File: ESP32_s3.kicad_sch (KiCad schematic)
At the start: 77 parts, among them J1 Conn_01x02_Pin, J10 TXRX2, J11 backup, J12 Conn_01x02_Pin, J13 jetsonnano, J14 Conn_01x03_Pin, J15 Conn_01x03_Pin, J2 programming header usb, J3 Conn_01x02, J4 Servo motor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

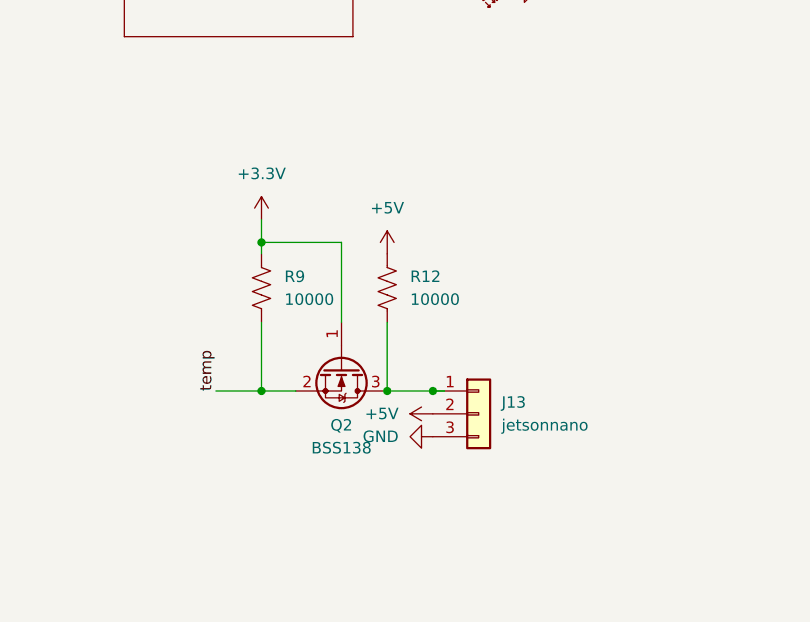
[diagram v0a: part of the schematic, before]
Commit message: Finished PCB Boost Layout
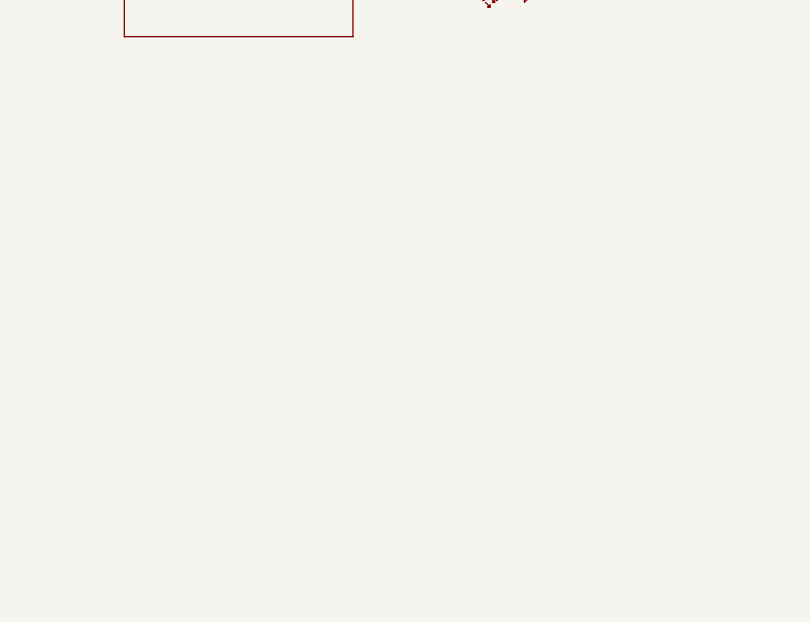
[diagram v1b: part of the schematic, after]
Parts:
- removed J13: jetsonnano, 61300311121:61300311121, symbol Connector_Generic:Conn_01x03
- removed Q2: BSS138, Package_TO_SOT_SMD:SOT-23, symbol Transistor_FET:BSS138
- removed R12, R9: 10000, RR1220P-1030-D:RESC2012X50N, symbol Device:R_US

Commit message: PCB update
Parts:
- added J13: Jetson Power Supply, 01x02connector:CONN_61300211121_WRE, symbol Connector:Conn_01x02_Pin
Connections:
- net +5V: no longer D10.1 (K), R11.1
- new net 5V: D10.1 (K), J13.1 (Pin_1), J13.2 (Pin_2), R11.1
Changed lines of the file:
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@@
 	)
 	(junction
+		(at 66.04 74.93)
+		(diameter 0)
+		(color 0 0 0 0)
+	)
+	(junction
 		(at 95.25 149.86)
 		(diameter 0)
@@
 	(wire
 		(pts
+			(xy 63.5 74.93) (xy 66.04 74.93)
+		)
+		(stroke
+			(width 0)
+			(type default)
+		)
+	)
+	(wire
+		(pts
 			(xy 254 215.9) (xy 248.92 215.9)
 		)
@@
 	(wire
 		(pts
+			(xy 66.04 76.2) (xy 66.04 74.93)
+		)
+		(stroke
+			(width 0)
+			(type default)
+		)
+	)
+	(wire
+		(pts
 			(xy 224.79 52.07) (xy 213.36 52.07)
 		)
@@
 	(wire
 		(pts
+			(xy 66.04 76.2) (xy 73.66 76.2)
+		)
+		(stroke
+			(width 0)
+			(type default)
+		)
+	)
+	(wire
+		(pts
 			(xy 182.88 152.4) (xy 180.34 152.4)
 		)
@@
 	(wire
 		(pts
+			(xy 66.04 74.93) (xy 66.04 73.66)
+		)
+		(stroke
+			(width 0)
+			(type default)
+		)
+	)
+	(wire
+		(pts
 			(xy 203.2 187.96) (xy 208.28 187.96)
 		)
@@
 	(wire
 		(pts
+			(xy 66.04 73.66) (xy 73.66 73.66)
+		)
+		(stroke
+			(width 0)
+			(type default)
+		)
+	)
+	(wire
+		(pts
 			(xy 133.35 36.83) (xy 146.05 36.83)
 		)
@@
 		)
 	)
+	(global_label "5V"
+		(shape input)
+		(at 63.5 74.93 180)
+		(fields_autoplaced yes)
+		(effects
+			(font
+				(size 1.27 1.27)
+			)
+			(justify right)
+		)
+		(property "Intersheetrefs" "${INTERSHEET_REFS}"
+			(at 58.2167 74.93 0)
+			(effects
+				(font
+					(size 1.27 1.27)
+				)
+				(justify right)
+				(hide yes)
+			)
+		)
+	)
 	(global_label "Vout"
 		(shape input)
@@
 		)
 	)
+	(global_label "5V"
+		(shape input)
+		(at 96.52 49.53 0)
+		(fields_autoplaced yes)
+		(effects
+			(font
+				(size 1.27 1.27)
+			)
+			(justify left)
+		)
+		(property "Intersheetrefs" "${INTERSHEET_REFS}"
+			(at 101.8033 49.53 0)
+			(effects
+				(font
+					(size 1.27 1.27)
+				)
+				(justify left)
+				(hide yes)
+			)
+		)
+	)
 	(global_label "Vin"
 		(shape input)
@@
 	)
 	(symbol
-		(lib_id "stm32f091-rescue:+5V-power")
-		(at 96.52 49.53 270)
-		(unit 1)
-		(exclude_from_sim no)
-		(in_bom yes)
-		(on_board yes)
-		(dnp no)
-		(property "Reference" "#PWR021"
-			(at 92.71 49.53 0)
-			(effects
-				(font
-					(size 1.27 1.27)
-				)
-				(hide yes)
-			)
-		)
-		(property "Value" "+5V"
-			(at 100.9142 49.911 0)
-			(effects
-				(font
-					(size 1.27 1.27)
-				)
-			)
-		)
-		(property "Footprint" ""
-			(at 96.52 49.53 0)
-			(effects
-				(font
-					(size 1.27 1.27)
-				)
-				(hide yes)
-			)
-		)
-		(property "Datasheet" ""
-			(at 96.52 49.53 0)
-			(effects
-				(font
-					(size 1.27 1.27)
-				)
-				(hide yes)
-			)
-		)
-		(property "Description" ""
-			(at 96.52 49.53 0)
-			(effects
-				(font
-					(size 1.27 1.27)
-				)
-				(hide yes)
-			)
-		)
-		(pin "1"
-		)
-		(instances
-			(project "ESP32_s3"
-				(path "/17b1a26b-4dd3-45da-ac9f-9f7d4372170f"
-					(reference "#PWR021")
-					(unit 1)
-				)
-			)
-		)
-	)
-	(symbol
 		(lib_id "Device:C")
 		(at 270.51 44.45 0)
@@
 					(unit 1)
 				)
+			)
+		)
+	)
+	(symbol
+		(lib_id "Connector:Conn_01x02_Pin")
+		(at 78.74 76.2 180)
+		(unit 1)
+		(exclude_from_sim no)
+		(in_bom yes)
+		(on_board yes)
+		(dnp no)
+		(property "Reference" "J13"
+			(at 80.01 73.6599 0)
+			(effects
+				(font
+					(size 1.27 1.27)
+				)
+				(justify right)
+				(hide yes)
+			)
+		)
+		(property "Value" "Jetson Power Supply"
+			(at 80.264 74.93 0)
+			(effects
+				(font
+					(size 1.27 1.27)
+				)
+				(justify right)
+			)
+		)
+		(property "Footprint" "01x02connector:CONN_61300211121_WRE"
+			(at 78.74 76.2 0)
+			(effects
+				(font
+					(size 1.27 1.27)
+				)
+				(hide yes)
+			)
+		)
+		(property "Datasheet" "~"
+			(at 78.74 76.2 0)
+			(effects
+				(font
+					(size 1.27 1.27)
+				)
+				(hide yes)
+			)
+		)
+		(property "Description" "Generic connector, single row, 01x02, script generated"
+			(at 78.74 76.2 0)
+			(effects
+				(font
+					(size 1.27 1.27)
+				)
+				(hide yes)
+			)
+		)
+		(pin "1"
+		)
+		(pin "2"
+		)
+		(instances
+			(project "ESP32_s3"
+				(path "/17b1a26b-4dd3-45da-ac9f-9f7d4372170f"
+					(reference "J13")
+					(unit 1)
+				)

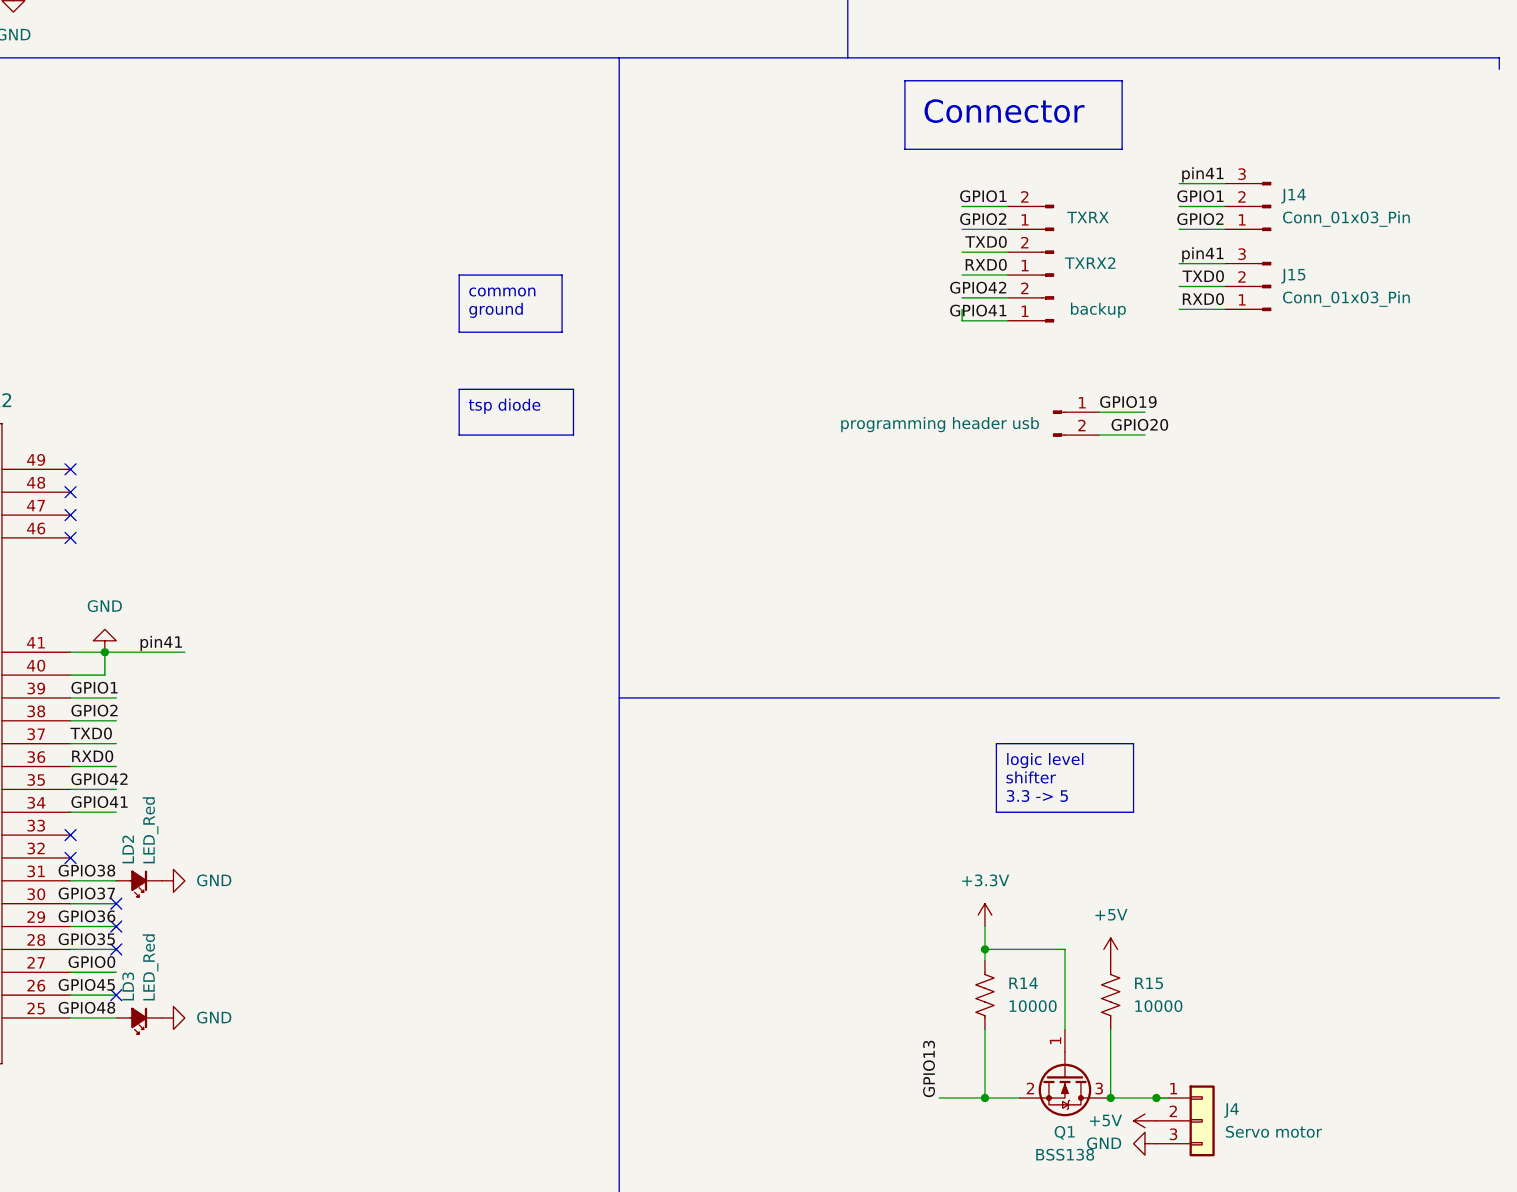
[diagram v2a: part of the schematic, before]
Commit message: add resistors to debugging led
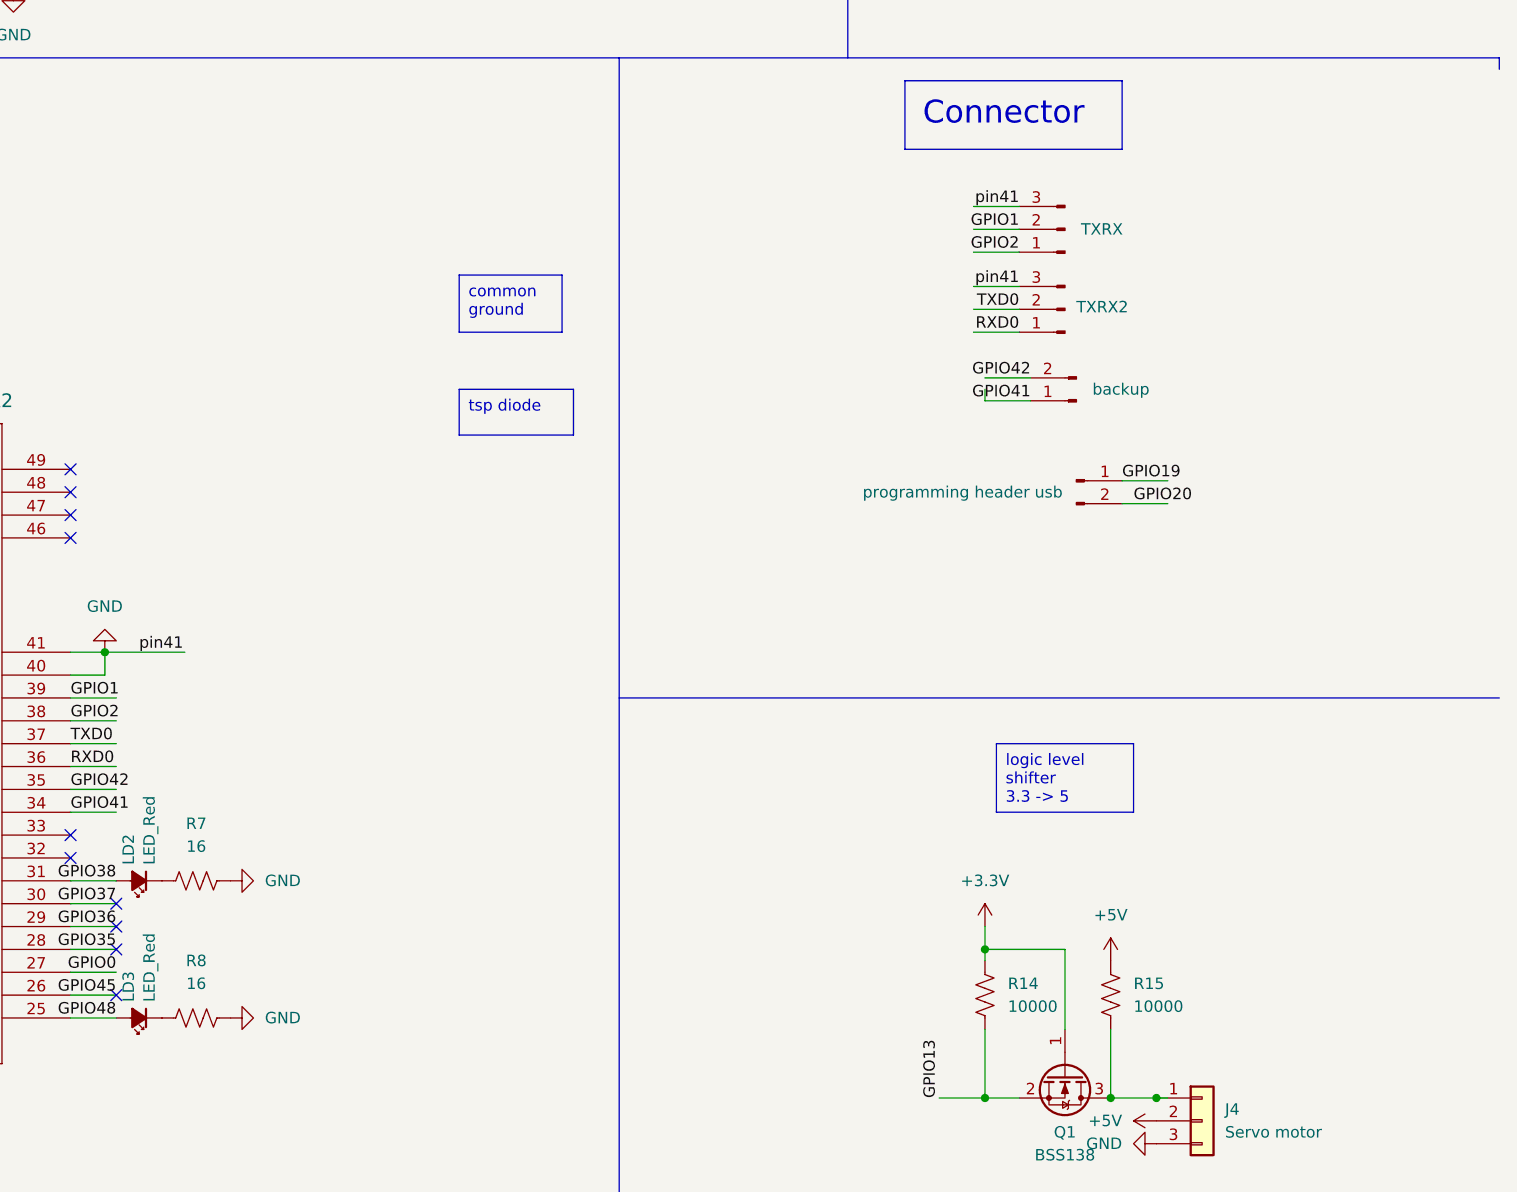
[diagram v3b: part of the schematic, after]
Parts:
- removed J10: TXRX2, 01x02connector:CONN_61300211121_WRE, symbol Connector:Conn_01x02_Pin
- removed J6: TXRX, 01x02connector:CONN_61300211121_WRE, symbol Connector:Conn_01x02_Pin
- added R7, R8: 16, CRGCQ0805F220R:RESC2012X65N, symbol Device:R_US
- J14: value Conn_01x03_Pin -> TXRX
- J15: value Conn_01x03_Pin -> TXRX2
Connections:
- net GND: now also R7.2, R8.2; no longer LD2.1 (K), LD3.1 (K)
- new net: LD2.1 (K), R7.1
- new net: LD3.1 (K), R8.1

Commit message: update PCB layout
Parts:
- R10, R4: value 0 -> 10k; footprint RMCF1206ZR0R00:RESC3216X70N -> CRCW080535K7FKEA:RESC2012X50N
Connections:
- net +3.3V: now also R10.2, R4.2; no longer C14.1, C2.1, R10.1, R4.1, SW1.2, SW2.2
- net EN: now also C14.1, R10.1, SW1.2; no longer R10.2
- net GPIO0: now also C2.1, R4.1, SW2.2; no longer R4.2
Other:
- moved on the sheet: R10, R4
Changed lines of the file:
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@@
 	)
 	(junction
+		(at 361.95 36.83)
+		(diameter 0)
+		(color 0 0 0 0)
+	)
+	(junction
 		(at 289.56 67.31)
 		(diameter 0)
@@
 	)
 	(junction
+		(at 361.95 60.96)
+		(diameter 0)
+		(color 0 0 0 0)
+	)
+	(junction
 		(at 204.47 97.79)
 		(diameter 0)
@@
 	(wire
 		(pts
-			(xy 358.14 60.96) (xy 361.95 60.96)
-		)
-		(stroke
-			(width 0)
-			(type default)
-		)
-	)
-	(wire
-		(pts
 			(xy 369.57 224.79) (xy 364.49 224.79)
 		)
@@
 	(wire
 		(pts
+			(xy 361.95 59.69) (xy 361.95 60.96)
+		)
+		(stroke
+			(width 0)
+			(type default)
+		)
+	)
+	(wire
+		(pts
 			(xy 224.79 36.83) (xy 213.36 36.83)
 		)
@@
 	(wire
 		(pts
+			(xy 361.95 35.56) (xy 361.95 36.83)
+		)
+		(stroke
+			(width 0)
+			(type default)
+		)
+	)
+	(wire
+		(pts
 			(xy 50.8 229.87) (xy 50.8 226.06)
 		)
@@
 	(wire
 		(pts
+			(xy 361.95 60.96) (xy 370.84 60.96)
+		)
+		(stroke
+			(width 0)
+			(type default)
+		)
+	)
+	(wire
+		(pts
 			(xy 58.42 226.06) (xy 66.04 226.06)
 		)
@@
 	(wire
 		(pts
-			(xy 369.57 60.96) (xy 374.65 60.96)
-		)
-		(stroke
-			(width 0)
-			(type default)
-		)
-	)
-	(wire
-		(pts
 			(xy 80.01 49.53) (xy 68.58 49.53)
 		)
@@
 	(wire
 		(pts
+			(xy 361.95 60.96) (xy 358.14 60.96)
+		)
+		(stroke
+			(width 0)
+			(type default)
+		)
+	)
+	(wire
+		(pts
 			(xy 359.41 208.28) (xy 350.52 208.28)
 		)
@@
 	(wire
 		(pts
+			(xy 361.95 36.83) (xy 372.11 36.83)
+		)
+		(stroke
+			(width 0)
+			(type default)
+		)
+	)
+	(wire
+		(pts
 			(xy 146.05 97.79) (xy 158.75 97.79)
 		)
@@
 	(wire
 		(pts
-			(xy 369.57 36.83) (xy 374.65 36.83)
-		)
-		(stroke
-			(width 0)
-			(type default)
-		)
-	)
-	(wire
-		(pts
 			(xy 275.59 67.31) (xy 260.35 67.31)
 		)
@@
 	)
 	(label "EN"
-		(at 372.11 36.83 0)
+		(at 369.57 36.83 0)
 		(fields_autoplaced yes)
 		(effects
@@
 	)
 	(label "GPIO0"
-		(at 372.11 60.96 0)
+		(at 370.84 60.96 0)
 		(fields_autoplaced yes)
 		(effects
@@
 	(symbol
 		(lib_id "Device:R_US")
-		(at 365.76 36.83 90)
+		(at 361.95 31.75 180)
 		(unit 1)
 		(exclude_from_sim no)
@@
 		(fields_autoplaced yes)
 		(property "Reference" "R10"
-			(at 365.76 30.48 90)
+			(at 364.49 30.4799 0)
 			(effects
 				(font
 					(size 1.27 1.27)
 				)
+				(justify right)
 			)
 		)
-		(property "Value" "0"
-			(at 365.76 33.02 90)
+		(property "Value" "10k"
+			(at 364.49 33.0199 0)
 			(effects
 				(font
 					(size 1.27 1.27)
 				)
+				(justify right)
 			)
 		)
-		(property "Footprint" "RMCF1206ZR0R00:RESC3216X70N"
-			(at 366.014 35.814 90)
+		(property "Footprint" "CRCW080535K7FKEA:RESC2012X50N"
+			(at 360.934 31.496 90)
 			(effects
 				(font
@@
 		)
 		(property "Datasheet" "https://www.seielect.com/catalog/sei-rmcf_rmcp.pdf"
-			(at 365.76 36.83 0)
+			(at 361.95 31.75 0)
 			(effects
 				(font
@@
 		)
 		(property "Description" "Resistor, US symbol"
-			(at 365.76 36.83 0)
+			(at 361.95 31.75 0)
 			(effects
 				(font
@@
 	(symbol
 		(lib_id "Device:R_US")
-		(at 365.76 60.96 90)
+		(at 361.95 55.88 180)
 		(unit 1)
 		(exclude_from_sim no)
@@
 		(fields_autoplaced yes)
 		(property "Reference" "R4"
-			(at 365.76 54.61 90)
+			(at 364.49 54.6099 0)
 			(effects
 				(font
 					(size 1.27 1.27)
 				)
+				(justify right)
 			)
 		)
-		(property "Value" "0"
-			(at 365.76 57.15 90)
+		(property "Value" "10k"
+			(at 364.49 57.1499 0)
 			(effects
 				(font
 					(size 1.27 1.27)
 				)
+				(justify right)
 			)
 		)
-		(property "Footprint" "RMCF1206ZR0R00:RESC3216X70N"
-			(at 366.014 59.944 90)
+		(property "Footprint" "CRCW080535K7FKEA:RESC2012X50N"
+			(at 360.934 55.626 90)
 			(effects
 				(font
@@
 		)
 		(property "Datasheet" "https://www.seielect.com/catalog/sei-rmcf_rmcp.pdf"
-			(at 365.76 60.96 0)
+			(at 361.95 55.88 0)
 			(effects
 				(font
@@
 		)
 		(property "Description" "Resistor, US symbol"
-			(at 365.76 60.96 0)
+			(at 361.95 55.88 0)
 			(effects
 				(font
@@
 		(lib_name "+3.3V_2")
 		(lib_id "power:+3.3V")
-		(at 358.14 36.83 0)
+		(at 361.95 27.94 0)
 		(unit 1)
 		(exclude_from_sim no)
@@
 		(on_board yes)
 		(dnp no)
-		(fields_autoplaced yes)
 		(property "Reference" "#PWR028"
-			(at 358.14 40.64 0)
+			(at 361.95 31.75 0)
 			(effects
 				(font
@@
 		)
 		(property "Value" "+3.3V"
-			(at 358.14 31.75 0)
+			(at 361.95 23.876 0)
 			(effects
 				(font
@@
 		)
 		(property "Footprint" ""
-			(at 358.14 36.83 0)
+			(at 361.95 27.94 0)
 			(effects
 				(font
@@
 		)
 		(property "Datasheet" ""
-			(at 358.14 36.83 0)
+			(at 361.95 27.94 0)
 			(effects
 				(font
@@
 		)
 		(property "Description" "Power symbol creates a global label with name \"+3.3V\""
-			(at 358.14 36.83 0)
+			(at 361.95 27.94 0)
 			(effects
 				(font
@@
 		(lib_name "+3.3V_2")
 		(lib_id "power:+3.3V")
-		(at 358.14 60.96 0)
+		(at 361.95 52.07 0)
 		(unit 1)
 		(exclude_from_sim no)
@@
 		(fields_autoplaced yes)
 		(property "Reference" "#PWR027"
-			(at 358.14 64.77 0)
+			(at 361.95 55.88 0)
 			(effects
 				(font
@@
 		)
 		(property "Value" "+3.3V"
-			(at 358.14 55.88 0)
+			(at 361.95 46.99 0)
 			(effects
 				(font
@@
 		)
 		(property "Footprint" ""
-			(at 358.14 60.96 0)
+			(at 361.95 52.07 0)
 			(effects
 				(font
@@
 		)
 		(property "Datasheet" ""
-			(at 358.14 60.96 0)
+			(at 361.95 52.07 0)
 			(effects
 				(font
@@
 		)
 		(property "Description" "Power symbol creates a global label with name \"+3.3V\""
-			(at 358.14 60.96 0)
+			(at 361.95 52.07 0)
 			(effects
 				(font
